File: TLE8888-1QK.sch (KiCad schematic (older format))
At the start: 36 parts, among them Q1 IPD30N06S2L-23, U2 TLE8888QK

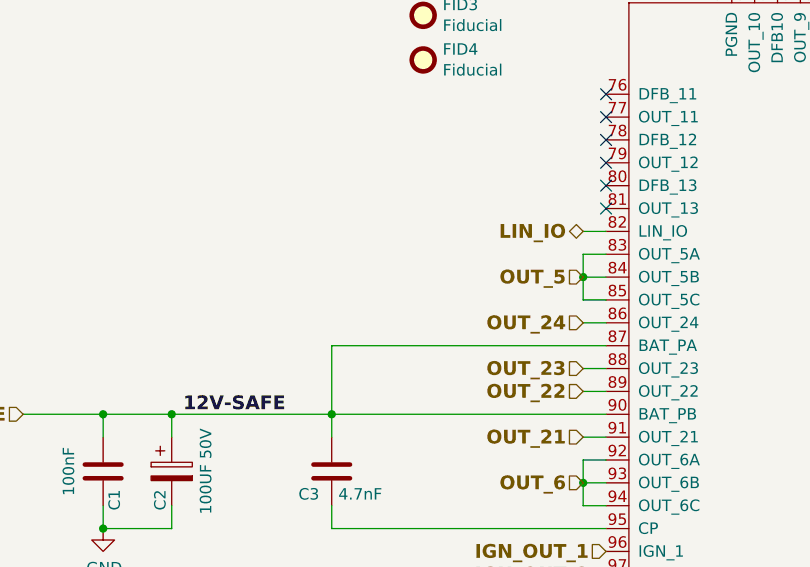
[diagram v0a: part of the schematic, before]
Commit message: Add diode and pull up on linbus. Fix some KiCAD 4.0 footprint problems
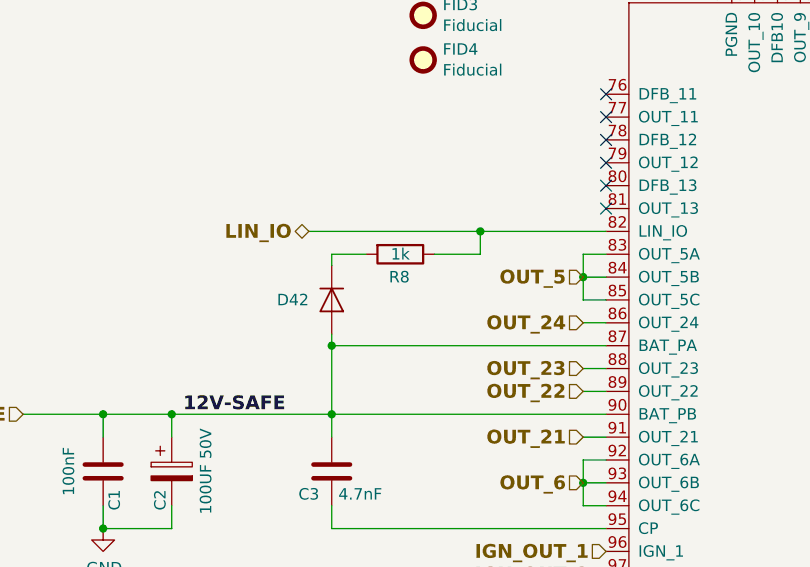
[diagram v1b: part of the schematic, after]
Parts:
- added D42: 1N4148WS, Diode_SMD:D_SOD-323, symbol Device:D
- added R8: 1k, Resistor_SMD:R_0603_1608Metric, symbol Device:R
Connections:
- net 12V_SAFE: now also D42.2 (A)
- net LIN_IO: now also R8.1
- new net: D42.1 (K), R8.2
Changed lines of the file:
@@
 Text HLabel 11675 10425 2    60   Output ~ 12
 LIN_RX
-Text HLabel 8000 7800 0    60   BiDi ~ 12
+Text HLabel 6800 7800 0    60   BiDi ~ 12
 LIN_IO
-Wire Wire Line
-	8100 7800 8000 7800
 $Comp
 L Diode:BAV70 D1
@@
 Text Label 8750 6700 1    50   ~ 10
 OUT_10
+$Comp
+L Device:D D?
+U 1 1 5DBFC8FC
+P 6900 8100
+AR Path="/5DBFC8FC" Ref="D?"  Part="1"
+AR Path="/5C5D7FA6/5DBFC8FC" Ref="D42"  Part="1"
+F 0 "D42" V 6900 8000 50  0000 R CNN
+F 1 "1N4148WS" H 7000 7975 50  0001 R CNN
+F 2 "Diode_SMD:D_SOD-323" H 6900 8100 50  0001 C CNN
+F 3 "~" H 6900 8100 50  0001 C CNN
+F 4 "NSR0530HT" H -4075 3425 50  0001 C CNN "Part #"
+F 5 "DIGI" H -4075 3425 50  0001 C CNN "VEND"
+F 6 "NSR0530HT1GOSCT-ND" H -4075 3425 50  0001 C CNN "VEND#"
+F 7 "ON-SEMI" H -4075 3425 50  0001 C CNN "Manufacturer"
+F 8 "C2128" H 6900 8100 50  0001 C CNN "LCSC"
+	1    6900 8100
+	0    1    1    0
+$EndComp
+Wire Wire Line
+	6900 8300 6900 8250
+Connection ~ 6900 8300
+$Comp
+L Device:R R?
+U 1 1 5DC1F576
+P 7200 7900
+AR Path="/5DC1F576" Ref="R?"  Part="1"
+AR Path="/5C5D7FA6/5DC1F576" Ref="R8"  Part="1"
+F 0 "R8" V 7300 7850 50  0000 L CNN
+F 1 "1k" V 7200 7900 50  0000 C CNN
+F 2 "Resistor_SMD:R_0603_1608Metric" V 7130 7900 50  0001 C CNN
+F 3 "~" H 7200 7900 50  0001 C CNN
+F 4 "StackPole" H -1125 1975 50  0001 C CNN "Manufacturer"
+F 5 "RMCF0603JJ1K00" H -1125 1975 50  0001 C CNN "Part #"
+F 6 "DIGI" H -1125 1975 50  0001 C CNN "VEND"
+F 7 "RMCF0603JJ1K00CT-ND" H -1125 1975 50  0001 C CNN "VEND#"
+F 8 "C21190" H 7200 7900 50  0001 C CNN "LCSC"
+	1    7200 7900
+	0    1    1    0
+$EndComp
+Wire Wire Line
+	6900 7900 7050 7900
+Wire Wire Line
+	7350 7900 7550 7900
+Wire Wire Line
+	7550 7900 7550 7800
+Connection ~ 7550 7800
+Wire Wire Line
+	7550 7800 8100 7800
+Wire Wire Line
+	6800 7800 7550 7800
+Wire Wire Line
+	6900 7950 6900 7900
 $EndSCHEMATC
